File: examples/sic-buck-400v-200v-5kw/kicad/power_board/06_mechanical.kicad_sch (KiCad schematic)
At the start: 22 parts

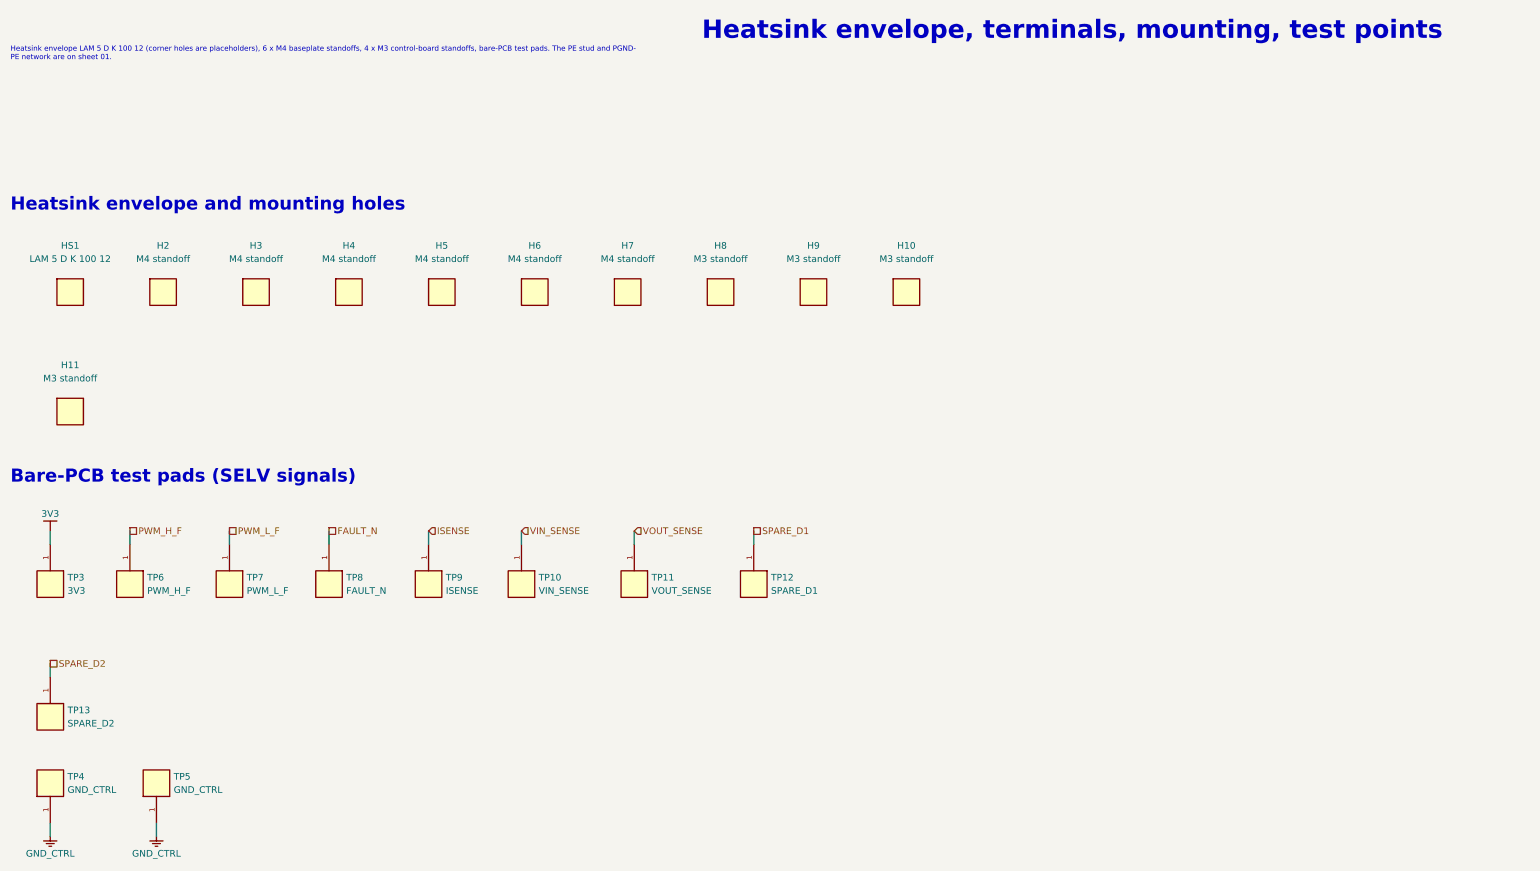
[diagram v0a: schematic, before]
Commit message: Correct sensing circuits and add verified V2.2 local bypasses
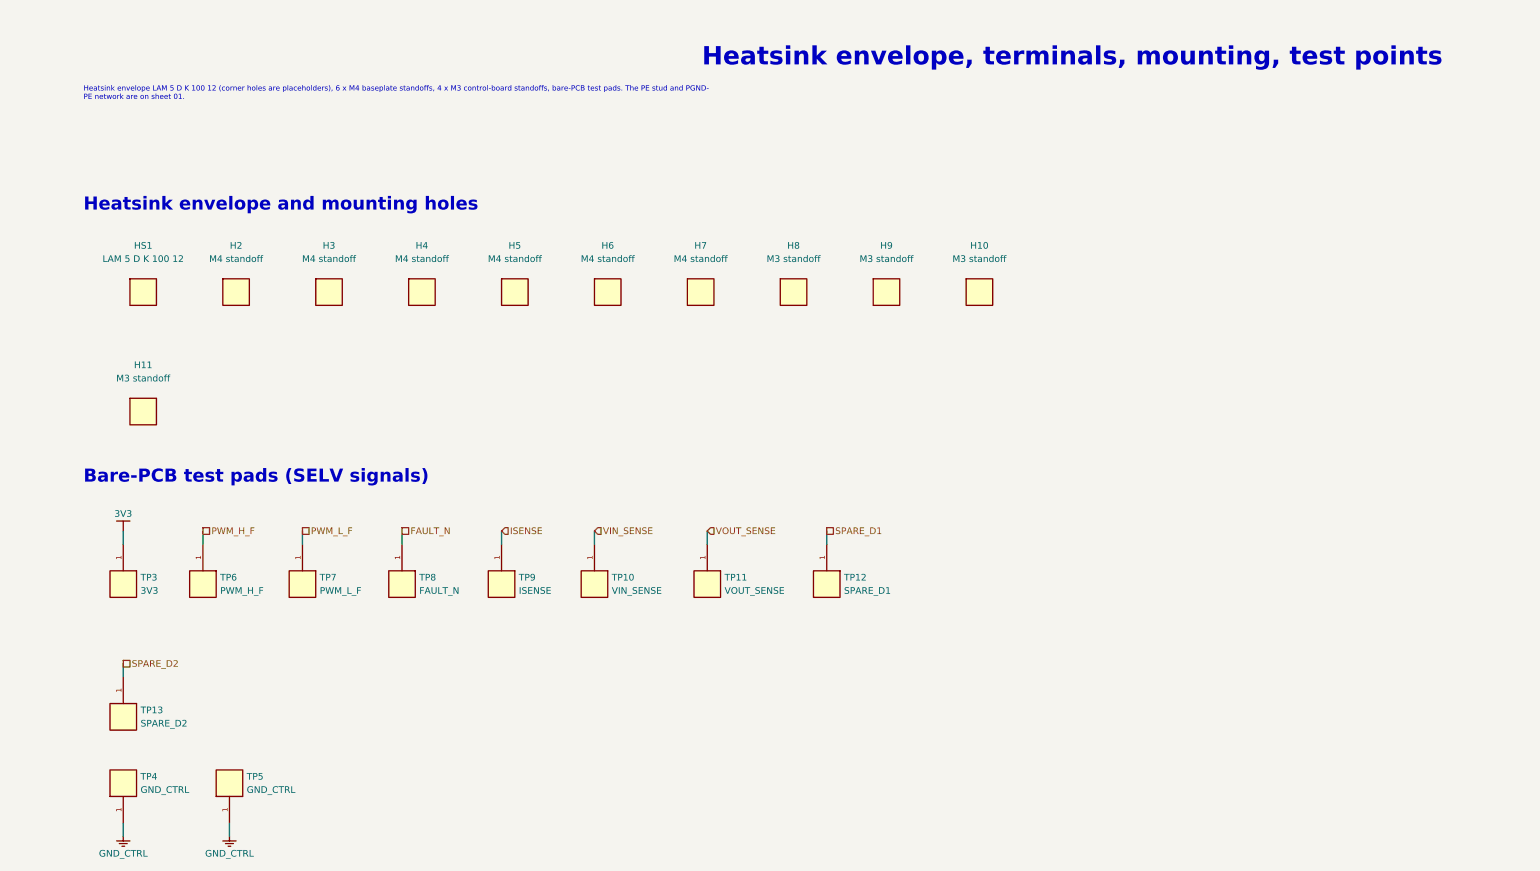
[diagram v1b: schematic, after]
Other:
- moved on the sheet: H10, H11, H2, H3, H4, H5, H6, H7, H8, H9, HS1, TP10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
